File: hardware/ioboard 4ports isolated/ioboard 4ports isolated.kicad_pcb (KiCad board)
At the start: 2 copper layers, 106 x 55 mm, 30 parts, among them J1 Conn_02x06_Odd_Even, J10 XLR3, J2 Conn_01x03, J3 XLR3, J4 Conn_01x03, J5 XLR3, J7 XLR3, U1 M24C02-WMN, U2 ADM2483xRW, U3 CRE1S0505DC, U4 ADM2483xRW

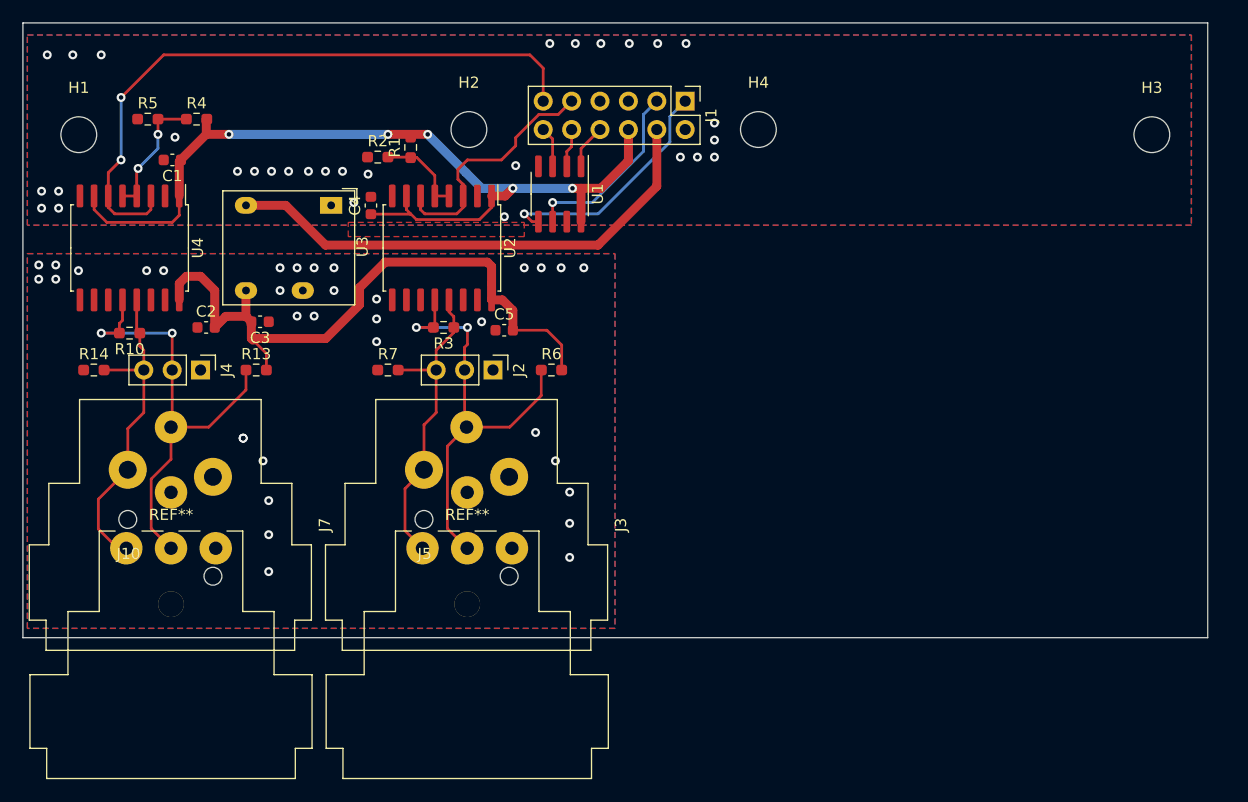
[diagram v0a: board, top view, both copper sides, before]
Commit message: Finish ioboard 4ports isolated
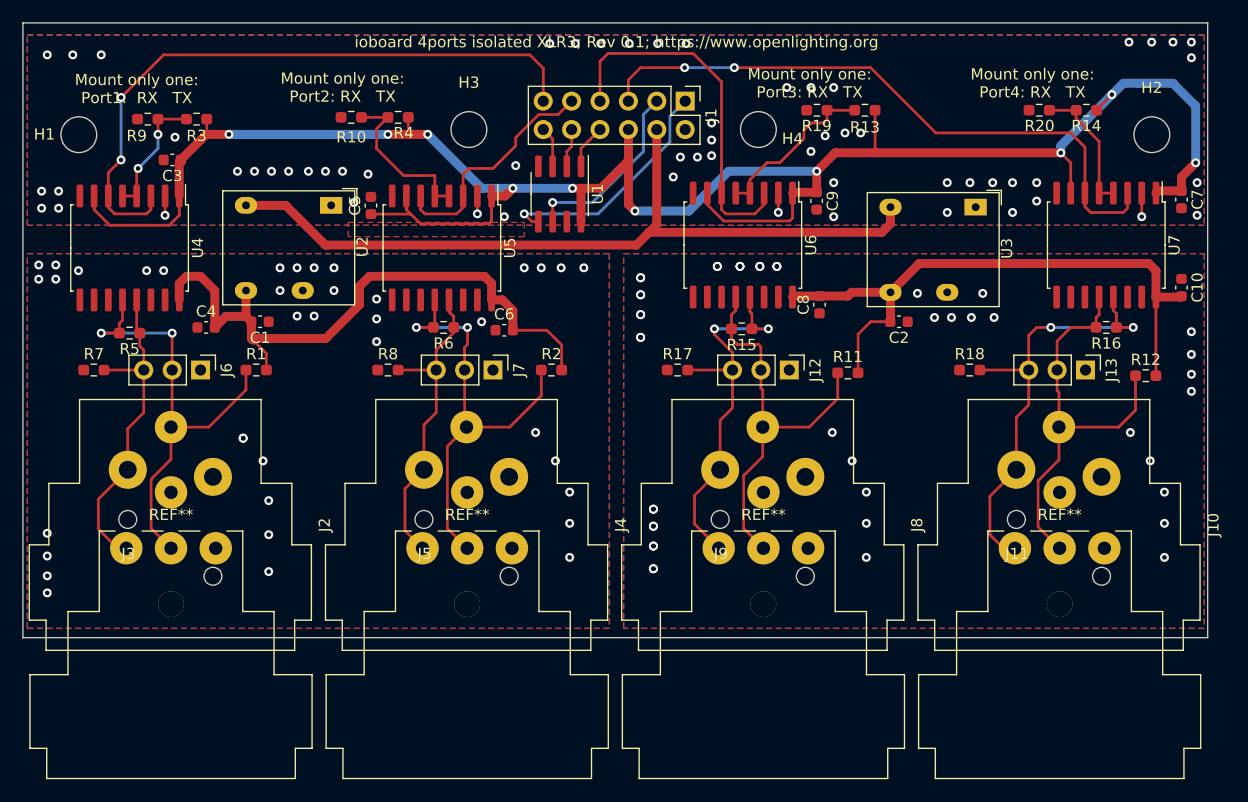
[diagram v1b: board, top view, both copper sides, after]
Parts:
- removed the J3 at (68.5, 60.6)
- added C10: 100nF, Capacitor_SMD:C_0603_1608Metric, F.Cu at (128.7, 43.7)
- added C2: 100nF, Capacitor_SMD:C_0603_1608Metric, F.Cu at (103.4, 46.7)
- added C7: 100nF, Capacitor_SMD:C_0603_1608Metric, F.Cu at (128.7, 35.8)
- added C8: 100nF, Capacitor_SMD:C_0603_1608Metric, F.Cu at (96.3, 45.2)
- added C9: 100nF, Capacitor_SMD:C_0603_1608Metric, F.Cu at (96.0, 35.9)
- added J10: XLR3, Connector_Audio:Jack_XLR_Neutrik_NC3FAAH_Horizontal, F.Cu at (121.5, 60.6)
- added J11: XLR3, NC3FD-H:Jack_XLR_Neutrik_NC3FD-H_Horizontal, F.Cu at (117.8, 67.0)
- added J12: Conn_01x03, Connector_PinHeader_2.54mm:PinHeader_1x03_P2.54mm_Vertical, F.Cu at (93.6, 51.1)
- added J13: Conn_01x03, Connector_PinHeader_2.54mm:PinHeader_1x03_P2.54mm_Vertical, F.Cu at (120.1, 51.1)
- added J4: XLR3, Connector_Audio:Jack_XLR_Neutrik_NC3FAAH_Horizontal, F.Cu at (68.5, 60.6)
- added J8: XLR3, Connector_Audio:Jack_XLR_Neutrik_NC3FAAH_Horizontal, F.Cu at (95.0, 60.6)
- added J9: XLR3, NC3FD-H:Jack_XLR_Neutrik_NC3FD-H_Horizontal, F.Cu at (91.2, 67.0)
- added R11: 680R, Resistor_SMD:R_0603_1608Metric_Pad0.98x0.95mm_HandSolder, F.Cu at (98.8, 51.3)
- added R12: 680R, Resistor_SMD:R_0603_1608Metric_Pad0.98x0.95mm_HandSolder, F.Cu at (125.5, 51.6)
- added R13: 0R, Resistor_SMD:R_0603_1608Metric_Pad0.98x0.95mm_HandSolder, F.Cu at (100.3, 27.8)
- added R14: 0R, Resistor_SMD:R_0603_1608Metric_Pad0.98x0.95mm_HandSolder, F.Cu at (120.1, 27.8)
- added R15: 120R, Resistor_SMD:R_0603_1608Metric_Pad0.98x0.95mm_HandSolder, F.Cu at (89.3, 47.4)
- added R16: 120R, Resistor_SMD:R_0603_1608Metric_Pad0.98x0.95mm_HandSolder, F.Cu at (121.9, 47.2)
- added R17: 680R, Resistor_SMD:R_0603_1608Metric_Pad0.98x0.95mm_HandSolder, F.Cu at (83.6, 51.1)
- added R18: 680R, Resistor_SMD:R_0603_1608Metric_Pad0.98x0.95mm_HandSolder, F.Cu at (109.7, 51.1)
- added R19: 0R-DO_NOT_MOUNT, Resistor_SMD:R_0603_1608Metric_Pad0.98x0.95mm_HandSolder, F.Cu at (96.0, 27.8)
- added R20: 0R-DO_NOT_MOUNT, Resistor_SMD:R_0603_1608Metric_Pad0.98x0.95mm_HandSolder, F.Cu at (115.9, 27.8)
- added U3: CRE1S0505DC, Converter_DCDC:Converter_DCDC_muRata_CRE1xxxxxxDC_THT, F.Cu at (110.2, 36.5)
- added U6: ADM2483xRW, Package_SO:SOIC-16W_7.5x10.3mm_P1.27mm, F.Cu at (89.4, 39.9)
- added U7: ADM2483xRW, Package_SO:SOIC-16W_7.5x10.3mm_P1.27mm, F.Cu at (121.9, 39.9)
- moved R10 4.27 mm to (54.4, 28.4)
- moved R4 2.91 mm to (58.6, 28.4), turned to 0 degrees
- renumbered C3 to C1, C1 to C3, C2 to C4, C4 to C5, C5 to C6, H3 to H2, H2 to H3, J7 to J2, J10 to J3, J4 to J6, J2 to J7, R13 to R1, R2 to R10, R6 to R2, R4 to R3, R1 to R4, R10 to R5, R3 to R6, R14 to R7, R7 to R8, R5 to R9, U3 to U2, U2 to U5
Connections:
- J1 pad 5: (no net) -> /GP3
- J1 pad 7: (no net) -> /GP2
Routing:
- net +3V3: track 82.2 -> 182.9 mm, vias 5 -> 10
- net /GP3: track 0.00 -> 57.0 mm, vias 0 -> 2
- net /VBUS_3+4: track 0.00 -> 55.2 mm
- net Net-(J10-Pad2): track 0.00 -> 40.4 mm, vias 0 -> 2
- net Net-(J10-Pad3): track 0.00 -> 37.6 mm
- net Net-(J12-Pad2): track 0.00 -> 36.4 mm
- net Net-(J12-Pad3): track 0.00 -> 35.8 mm, vias 0 -> 2
- net /GP2: track 0.00 -> 32.5 mm
- net +5V: track 45.5 -> 70.9 mm
- net Net-(R13-Pad1): track 0.00 -> 15.4 mm
- net Net-(R14-Pad1): track 0.00 -> 11.9 mm
- net Net-(R10-Pad2): track 7.97 -> 14.9 mm
- net GND: track 0.00 -> 6.79 mm, vias 30 -> 59
- net /GP1: track 23.2 -> 21.2 mm
- net /VBUS_1+2: track 59.4 -> 57.5 mm
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- added copper zone on B.Cu, net /GND_3+4
- added copper zone on F.Cu, net /GND_3+4
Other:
- board text added: "Mount only one: Port1: RX TX"
- board text added: "Mount only one: Port2: RX TX"
- board text added: "Mount only one: Port3: RX TX"
- board text added: "Mount only one: Port4: RX TX"
- board text added: "ioboard 4ports isolated XLR3; Rev 0.1; https://www.openlighting.org"

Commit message: Hardware: Several fixes and improvements in schematics and PCBs (more capacitors, alternative footprint for DC/DC converter, more GND stitching, better trace placement, ...)
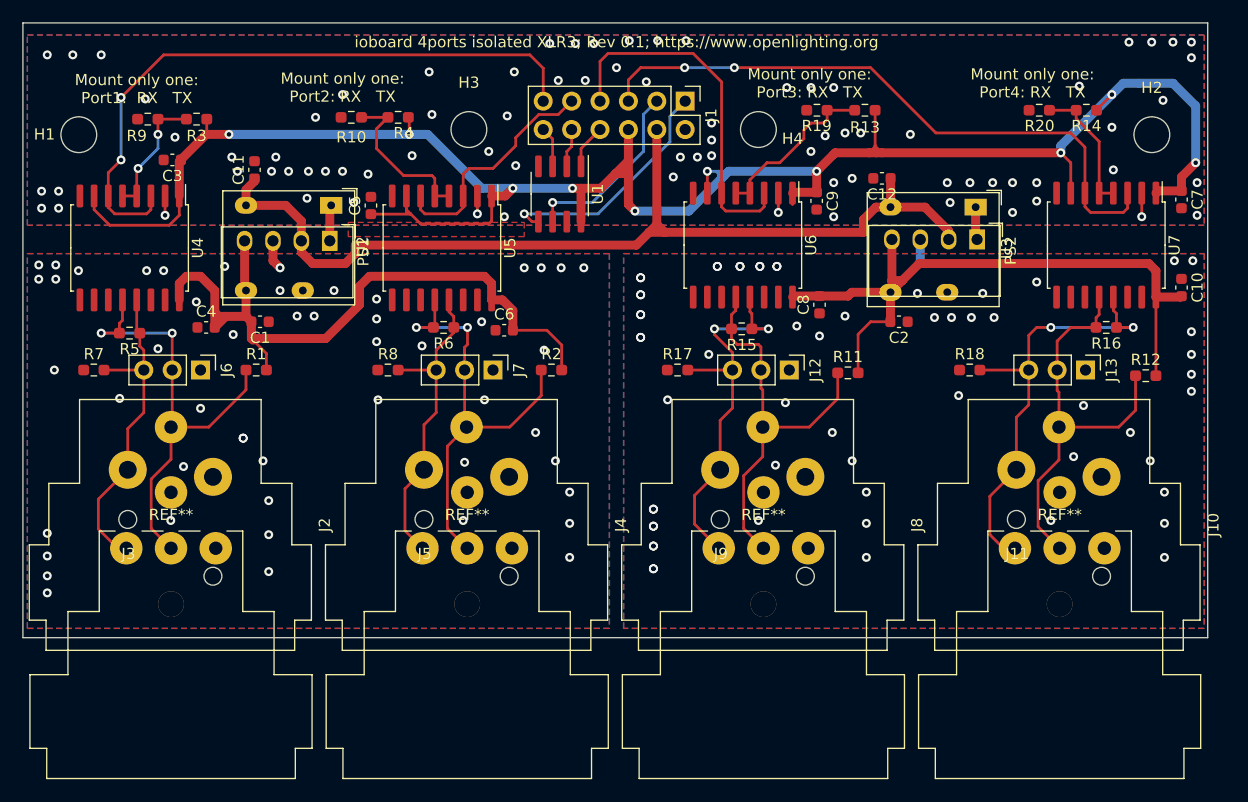
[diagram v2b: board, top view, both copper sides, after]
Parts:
- added C11: 100nF, Capacitor_SMD:C_0603_1608Metric, F.Cu at (45.7, 33.1)
- added C12: 100nF, Capacitor_SMD:C_0603_1608Metric, F.Cu at (101.9, 33.9)
- added PS1: MEE1S0503SC, Converter_DCDC:Converter_DCDC_muRata_CRE1xxxxxx3C_THT, F.Cu at (52.5, 39.5)
- added PS2: MEE1S0503SC, Converter_DCDC:Converter_DCDC_muRata_CRE1xxxxxx3C_THT, F.Cu at (110.4, 39.4)
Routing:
- net +5V: track 70.9 -> 87.3 mm
- net GND: track 6.79 -> 13.0 mm, vias 59 -> 80
- net /VBUS_3+4: track 55.2 -> 60.9 mm
- net /VBUS_1+2: track 57.5 -> 63.1 mm
- net +3V3: track 182.9 -> 180.0 mm
- net /GND_1+2: track 0.00 -> 2.68 mm, vias 38 -> 50
- net /GND_3+4: track 0.00 -> 2.16 mm, vias 44 -> 59

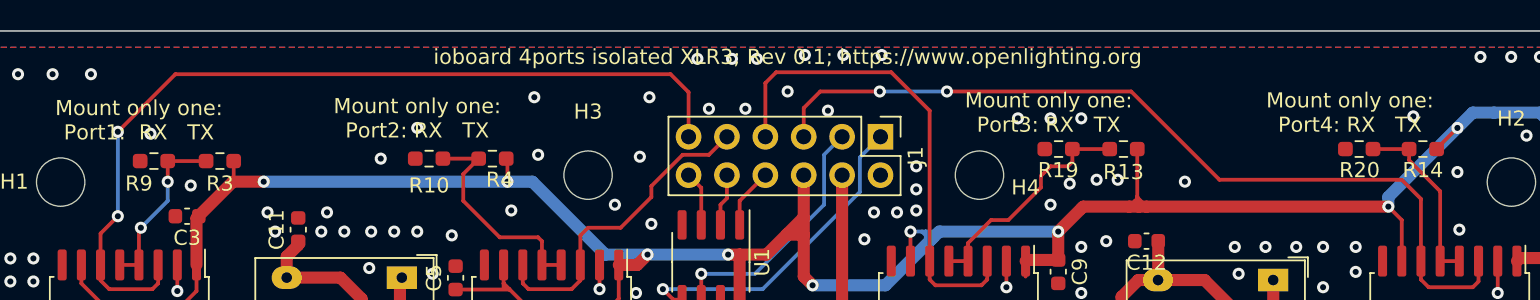
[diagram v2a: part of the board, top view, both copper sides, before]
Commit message: Add LCSC part numbers to the schematic for production :)
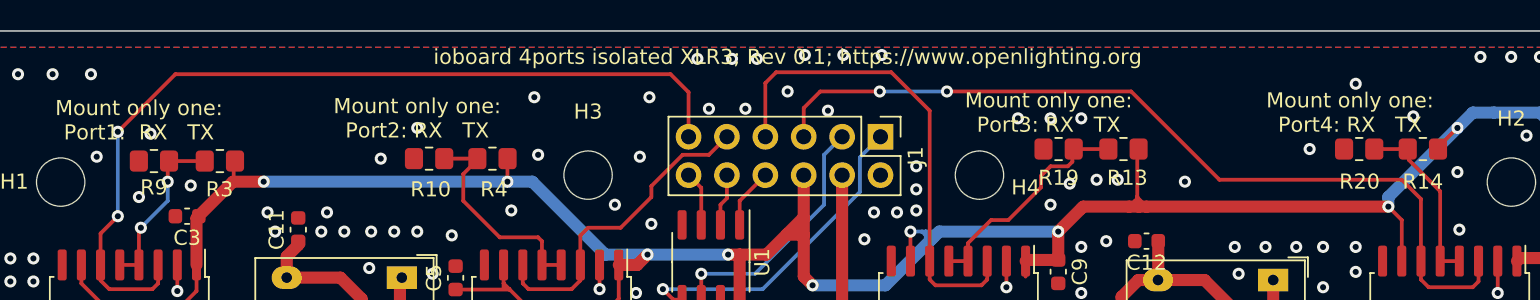
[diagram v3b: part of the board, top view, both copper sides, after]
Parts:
- R10, R13, R14, R19, R20, R3, R4, R9: footprint Resistor_SMD:R_0603_1608Metric_Pad0.98x0.95mm_HandSolder -> Resistor_SMD:R_0805_2012Metric_Pad1.20x1.40mm_HandSolder
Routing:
- net GND: vias 80 -> 84
